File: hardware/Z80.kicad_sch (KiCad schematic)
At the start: 24 parts, among them J1 RP2040 SWD, SW1 Reset, U1 Pico, U2 SN74HC165N, U3 SN74HC165N, U4 Z80CPU

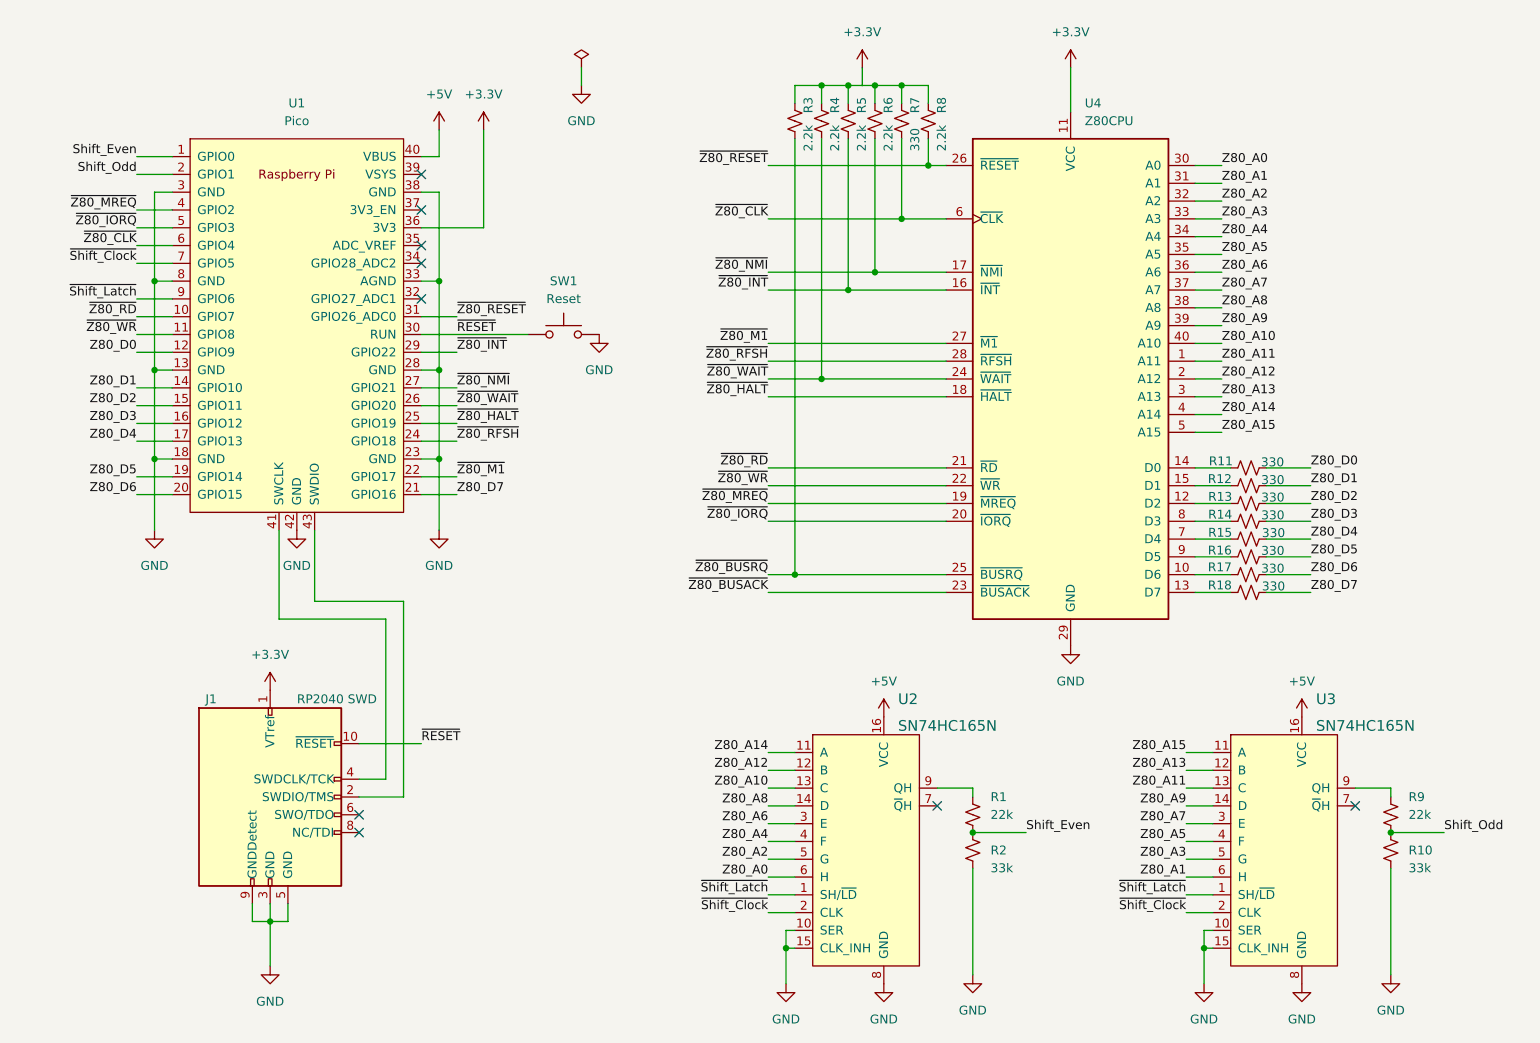
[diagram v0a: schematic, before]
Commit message: Initial firmware commit
This is a simple little program that makes sure that the RP2040 and its
PIO hardware can be used to clock the Z80 microprocessor and satisfy
its memory requests. It runs a simple Z80 program that increments a
16-bit counter in a loop and verifies that this counter is incremented
as expected.

* Updated README to cover the latest developments on this project.
* Updated schematic with changes that I found I had to make once I had
  it prototyped on a breadboard and started writing the PIO state
  machine code.
* Only running the Z80 at 1kHz with the firmware in this commit but it
  can run faster. The maximum frequency is currently limited by the
  shift registers and that is around 400kHz. The RP2040 code itself
  will probably introduce a limit somewhere between 2 and 3MHz.
* The code can be vastly improved but this code is far enough along
  that I feel it is safe for me to design a PCB around the current
  schematic and have it fabricated so that I move away from the
  breadboard implementation.
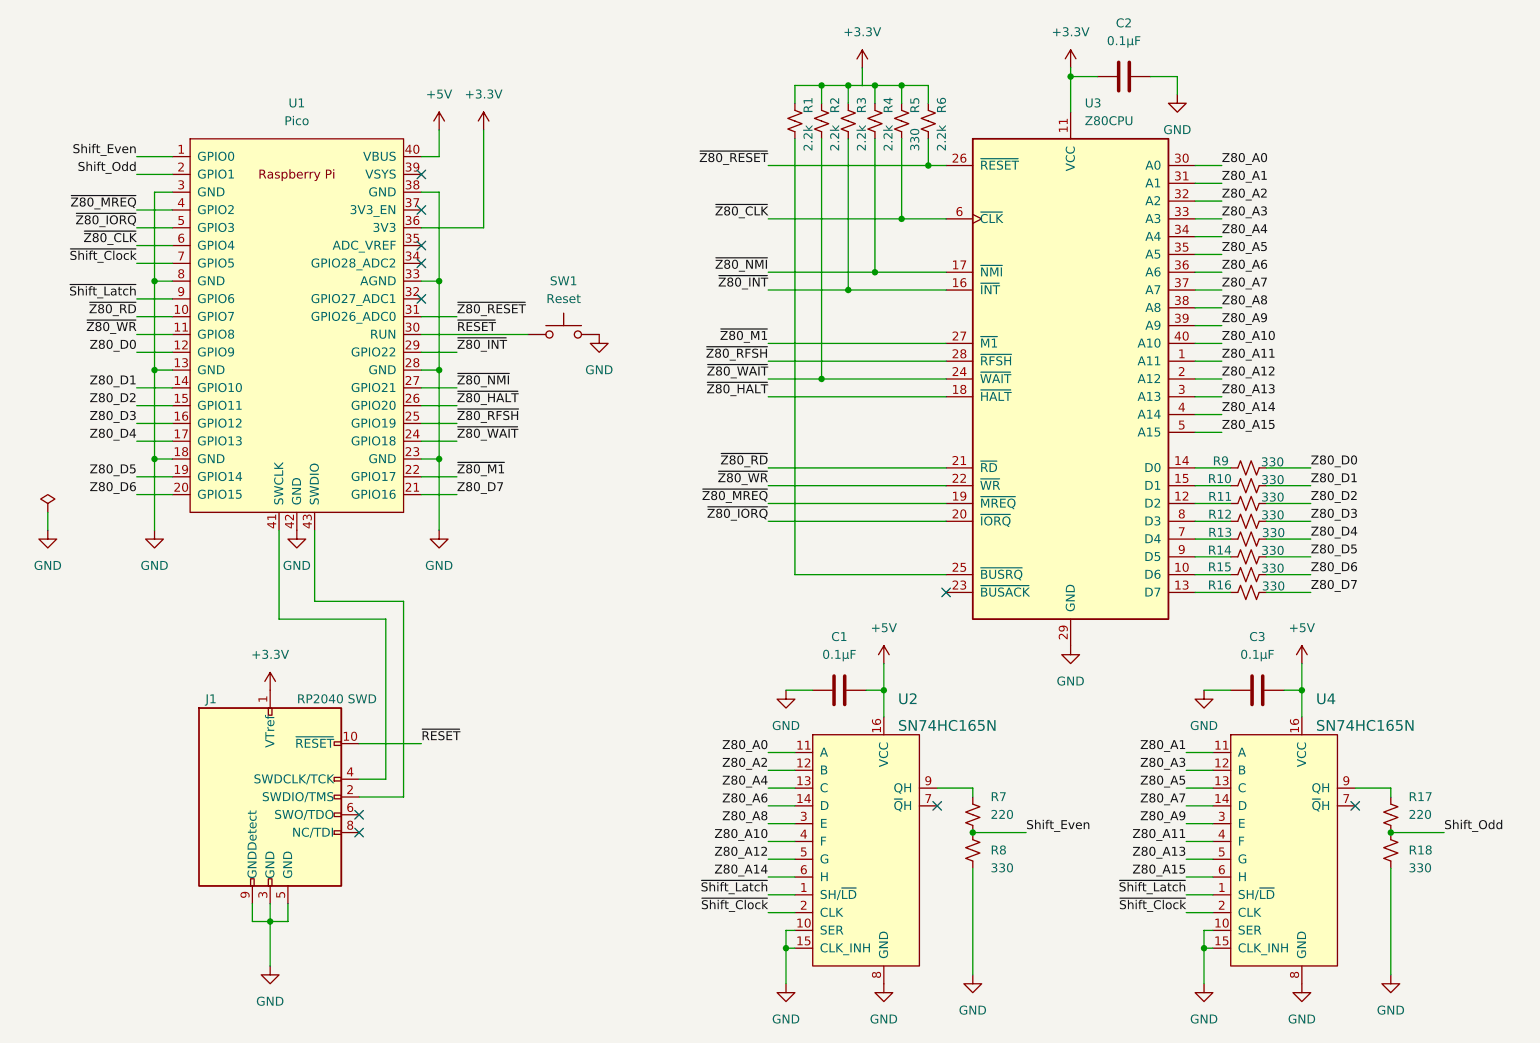
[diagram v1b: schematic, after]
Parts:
- added C1, C2, C3: 0.1µF, symbol Device:C
- R17: renamed from R9; value 22k -> 220
- R18: renamed from R10; value 33k -> 330
- R7: renamed from R1; value 22k -> 220
- R8: renamed from R2; value 33k -> 330
- renumbered R3 to R1, R12 to R10, R13 to R11, R14 to R12, R15 to R13, R16 to R14, R17 to R15, R18 to R16, R4 to R2, R5 to R3, R6 to R4, R7 to R5, R8 to R6, R11 to R9, U4 to U3, U3 to U4
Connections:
- net +3.3V: now also C2.1
- net +5V: now also C1.2, C3.2
- net GND: now also C1.1, C2.2, C3.1
- net Z80_A0: now also U2.11 (A); no longer U2.6 (H)
- net Z80_A1: now also U4.11 (A); no longer U4.6 (H)
- net Z80_A10: now also U2.4 (F); no longer U2.13 (C)
- net Z80_A11: now also U4.4 (F); no longer U4.13 (C)
- net Z80_A12: now also U2.5 (G); no longer U2.12 (B)
- net Z80_A13: now also U4.5 (G); no longer U4.12 (B)
- net Z80_A14: now also U2.6 (H); no longer U2.11 (A)
- net Z80_A15: now also U4.6 (H); no longer U4.11 (A)
- net Z80_A2: now also U2.12 (B); no longer U2.5 (G)
- net Z80_A3: now also U4.12 (B); no longer U4.5 (G)
- net Z80_A4: now also U2.13 (C); no longer U2.4 (F)
- net Z80_A5: now also U4.13 (C); no longer U4.4 (F)
- net Z80_A6: now also U2.14 (D); no longer U2.3 (E)
- net Z80_A7: now also U4.14 (D); no longer U4.3 (E)
- net Z80_A8: now also U2.3 (E); no longer U2.14 (D)
- net Z80_A9: now also U4.3 (E); no longer U4.14 (D)
- net ~{Z80_HALT}: now also U1.26 (GPIO20); no longer U1.25 (GPIO19)
- net ~{Z80_RFSH}: now also U1.25 (GPIO19); no longer U1.24 (GPIO18)
- net ~{Z80_WAIT}: now also U1.24 (GPIO18); no longer U1.26 (GPIO20)
- net ~{Z80_BUSACK}: no longer names the net of U3.23 (~{BUSACK})
- net ~{Z80_BUSRQ}: no longer names the net of R1.2, U3.25 (~{BUSRQ})
- no-connect marks 9 -> 10

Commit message: Update schematic
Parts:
- removed R5: 330, symbol Device:R_Small_US
- renumbered R11 to R10, R12 to R11, R13 to R12, R14 to R13, R15 to R14, R16 to R15, R17 to R16, R18 to R17, R6 to R5, R7 to R6, R8 to R7, R9 to R8, R10 to R9
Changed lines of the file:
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@@
   (junction (at 180.34 38.1) (diameter 0) (color 0 0 0 0)
   )
-  (junction (at 176.53 45.72) (diameter 0) (color 0 0 0 0)
-  )
   (junction (at 165.1 26.67) (diameter 0) (color 0 0 0 0)
   )
@@
   )
   (junction (at 168.91 26.67) (diameter 0) (color 0 0 0 0)
-  )
-  (junction (at 176.53 26.67) (diameter 0) (color 0 0 0 0)
   )
   (junction (at 160.02 149.86) (diameter 0) (color 0 0 0 0)
@@
     (stroke (width 0) (type default) (color 0 0 0 0))
   )
-  (wire (pts (xy 176.53 45.72) (xy 182.88 45.72))
-    (stroke (width 0) (type default) (color 0 0 0 0))
-  )
   (wire (pts (xy 110.49 36.83) (xy 110.49 33.02))
     (stroke (width 0) (type default) (color 0 0 0 0))
@@
     (stroke (width 0) (type default) (color 0 0 0 0))
   )
-  (wire (pts (xy 176.53 34.29) (xy 176.53 45.72))
-    (stroke (width 0) (type default) (color 0 0 0 0))
-  )
   (wire (pts (xy 217.17 134.62) (xy 220.98 134.62))
     (stroke (width 0) (type default) (color 0 0 0 0))
@@
     (stroke (width 0) (type default) (color 0 0 0 0))
   )
-  (wire (pts (xy 176.53 26.67) (xy 176.53 29.21))
-    (stroke (width 0) (type default) (color 0 0 0 0))
-  )
   (wire (pts (xy 157.48 124.46) (xy 161.29 124.46))
     (stroke (width 0) (type default) (color 0 0 0 0))
@@
     (stroke (width 0) (type default) (color 0 0 0 0))
   )
-  (wire (pts (xy 176.53 26.67) (xy 172.72 26.67))
+  (wire (pts (xy 172.72 26.67) (xy 180.34 26.67))
     (stroke (width 0) (type default) (color 0 0 0 0))
   )
@@
     (stroke (width 0) (type default) (color 0 0 0 0))
   )
-  (wire (pts (xy 180.34 26.67) (xy 176.53 26.67))
-    (stroke (width 0) (type default) (color 0 0 0 0))
-  )
   (wire (pts (xy 157.48 127) (xy 161.29 127))
     (stroke (width 0) (type default) (color 0 0 0 0))
@@
     (stroke (width 0) (type default) (color 0 0 0 0))
   )
-  (wire (pts (xy 157.48 45.72) (xy 176.53 45.72))
+  (wire (pts (xy 157.48 45.72) (xy 182.88 45.72))
     (stroke (width 0) (type default) (color 0 0 0 0))
   )
@@
   (symbol (lib_id "Device:R_Small_US") (at 226.06 83.82 90) (unit 1)
     (in_bom yes) (on_board yes)
-    (property "Reference" "R10" (id 0) (at 221.9687 82.8574 90))
+    (property "Reference" "R9" (id 0) (at 221.9687 82.8574 90))
     (property "Value" "330" (id 1) (at 229.5364 82.9985 90))
     (property "Footprint" "" (id 2) (at 226.06 83.82 0)
@@
   (symbol (lib_id "Device:R_Small_US") (at 226.06 99.06 90) (unit 1)
     (in_bom yes) (on_board yes)
-    (property "Reference" "R16" (id 0) (at 221.9687 98.0399 90))
+    (property "Reference" "R15" (id 0) (at 221.9687 98.0399 90))
     (property "Value" "330" (id 1) (at 229.6304 98.1809 90))
     (property "Footprint" "" (id 2) (at 226.06 99.06 0)
@@
   (symbol (lib_id "Device:R_Small_US") (at 246.38 135.89 0) (unit 1)
     (in_bom yes) (on_board yes)
-    (property "Reference" "R18" (id 0) (at 248.92 135.89 0)
+    (property "Reference" "R17" (id 0) (at 248.92 135.89 0)
       (effects (font (size 1.27 1.27)) (justify left))
     )
@@
   (symbol (lib_id "Device:R_Small_US") (at 186.69 135.89 0) (unit 1)
     (in_bom yes) (on_board yes)
-    (property "Reference" "R8" (id 0) (at 189.23 135.89 0)
+    (property "Reference" "R7" (id 0) (at 189.23 135.89 0)
       (effects (font (size 1.27 1.27)) (justify left))
     )
@@
   (symbol (lib_id "Device:R_Small_US") (at 180.34 31.75 0) (unit 1)
     (in_bom yes) (on_board yes)
-    (property "Reference" "R6" (id 0) (at 182.259 30.6376 90)
+    (property "Reference" "R5" (id 0) (at 182.259 30.6376 90)
       (effects (font (size 1.27 1.27)) (justify left))
     )
@@
   (symbol (lib_id "Device:R_Small_US") (at 226.06 81.28 90) (unit 1)
     (in_bom yes) (on_board yes)
-    (property "Reference" "R9" (id 0) (at 222.1097 80.3192 90))
+    (property "Reference" "R8" (id 0) (at 222.1097 80.3192 90))
     (property "Value" "330" (id 1) (at 229.4894 80.4602 90))
     (property "Footprint" "" (id 2) (at 226.06 81.28 0)
@@
   (symbol (lib_id "Device:R_Small_US") (at 226.06 86.36 90) (unit 1)
     (in_bom yes) (on_board yes)
-    (property "Reference" "R11" (id 0) (at 222.0157 85.3957 90))
+    (property "Reference" "R10" (id 0) (at 222.0157 85.3957 90))
     (property "Value" "330" (id 1) (at 229.5364 85.4897 90))
     (property "Footprint" "" (id 2) (at 226.06 86.36 0)
@@
   (symbol (lib_id "Device:R_Small_US") (at 226.06 96.52 90) (unit 1)
     (in_bom yes) (on_board yes)
-    (property "Reference" "R15" (id 0) (at 221.9687 95.4547 90))
+    (property "Reference" "R14" (id 0) (at 221.9687 95.4547 90))
     (property "Value" "330" (id 1) (at 229.5364 95.6427 90))
     (property "Footprint" "" (id 2) (at 226.06 96.52 0)
@@
   (symbol (lib_id "Device:R_Small_US") (at 186.69 130.81 0) (unit 1)
     (in_bom yes) (on_board yes)
-    (property "Reference" "R7" (id 0) (at 189.23 128.27 0)
+    (property "Reference" "R6" (id 0) (at 189.23 128.27 0)
       (effects (font (size 1.27 1.27)) (justify left))
     )
@@
   (symbol (lib_id "Device:R_Small_US") (at 226.06 93.98 90) (unit 1)
     (in_bom yes) (on_board yes)
-    (property "Reference" "R14" (id 0) (at 221.9687 93.0574 90))
+    (property "Reference" "R13" (id 0) (at 221.9687 93.0574 90))
     (property "Value" "330" (id 1) (at 229.5364 93.1044 90))
     (property "Footprint" "" (id 2) (at 226.06 93.98 0)
@@
     (pin "1")
   )
-  (symbol (lib_id "Device:R_Small_US") (at 176.53 31.75 0) (unit 1)
-    (in_bom yes) (on_board yes)
-    (property "Reference" "R5" (id 0) (at 178.449 30.6376 90)
-      (effects (font (size 1.27 1.27)) (justify left))
-    )
-    (property "Value" "330" (id 1) (at 178.449 36.0748 90)
-      (effects (font (size 1.27 1.27)) (justify left))
-    )
-    (property "Footprint" "" (id 2) (at 176.53 31.75 0)
-      (effects (font (size 1.27 1.27)) hide)
-    )
-    (property "Datasheet" "~" (id 3) (at 176.53 31.75 0)
-      (effects (font (size 1.27 1.27)) hide)
-    )
-    (pin "1")
-    (pin "2")
-  )
   (symbol (lib_id "Device:R_Small_US") (at 226.06 91.44 90) (unit 1)
     (in_bom yes) (on_board yes)
-    (property "Reference" "R13" (id 0) (at 222.0157 90.5192 90))
+    (property "Reference" "R12" (id 0) (at 222.0157 90.5192 90))
     (property "Value" "330" (id 1) (at 229.6304 90.5662 90))
     (property "Footprint" "" (id 2) (at 226.06 91.44 0)
@@
   (symbol (lib_id "Device:R_Small_US") (at 246.38 130.81 0) (unit 1)
     (in_bom yes) (on_board yes)
-    (property "Reference" "R17" (id 0) (at 248.92 128.27 0)
+    (property "Reference" "R16" (id 0) (at 248.92 128.27 0)
       (effects (font (size 1.27 1.27)) (justify left))
     )
@@
   (symbol (lib_id "Device:R_Small_US") (at 226.06 88.9 90) (unit 1)
     (in_bom yes) (on_board yes)
-    (property "Reference" "R12" (id 0) (at 222.0157 87.9339 90))
+    (property "Reference" "R11" (id 0) (at 222.0157 87.9339 90))
     (property "Value" "330" (id 1) (at 229.5364 88.0279 90))
     (property "Footprint" "" (id 2) (at 226.06 88.9 0)
@@
       (reference "R4") (unit 1) (value "2.2k") (footprint "")
     )
-    (path "/cb47eb21-f040-4a40-a689-d6b0ddf769fa"
-      (reference "R5") (unit 1) (value "330") (footprint "")
-    )
     (path "/4d5dd215-58fa-42fb-b48d-aae8a2cb4b7b"
-      (reference "R6") (unit 1) (value "2.2k") (footprint "")
+      (reference "R5") (unit 1) (value "2.2k") (footprint "")
     )
     (path "/ab03a96a-589d-4905-bd0c-4425f3417fb6"
-      (reference "R7") (unit 1) (value "220") (footprint "")
+      (reference "R6") (unit 1) (value "220") (footprint "")
     )
     (path "/4c05fbcf-e16b-4fd5-a5b1-a43636fa6dc3"
+      (reference "R7") (unit 1) (value "330") (footprint "")
+    )
+    (path "/5bae8d7f-a215-4306-b303-12041ae1d9dd"
       (reference "R8") (unit 1) (value "330") (footprint "")
     )
-    (path "/5bae8d7f-a215-4306-b303-12041ae1d9dd"
+    (path "/29967022-0716-413a-ae37-d82856be92e4"
       (reference "R9") (unit 1) (value "330") (footprint "")
     )
-    (path "/29967022-0716-413a-ae37-d82856be92e4"
+    (path "/96e68a8f-6e74-4e08-8f85-1adc6029fb52"
       (reference "R10") (unit 1) (value "330") (footprint "")
     )
-    (path "/96e68a8f-6e74-4e08-8f85-1adc6029fb52"
+    (path "/ff2ab6fa-a536-41a2-967e-8798d3665a42"
       (reference "R11") (unit 1) (value "330") (footprint "")
     )
-    (path "/ff2ab6fa-a536-41a2-967e-8798d3665a42"
+    (path "/cfa47cbe-c711-4d7b-b1fb-ed6f496e968d"
       (reference "R12") (unit 1) (value "330") (footprint "")
     )
-    (path "/cfa47cbe-c711-4d7b-b1fb-ed6f496e968d"
+    (path "/b3a77dbd-5397-4860-86c3-f296c00c8887"
       (reference "R13") (unit 1) (value "330") (footprint "")
     )
-    (path "/b3a77dbd-5397-4860-86c3-f296c00c8887"
+    (path "/a67dbef9-d4bd-4d26-9e93-58134f77470d"
       (reference "R14") (unit 1) (value "330") (footprint "")
     )
-    (path "/a67dbef9-d4bd-4d26-9e93-58134f77470d"
+    (path "/2aedb671-8989-4b47-ad64-1185ff3636e4"
       (reference "R15") (unit 1) (value "330") (footprint "")
     )
-    (path "/2aedb671-8989-4b47-ad64-1185ff3636e4"
-      (reference "R16") (unit 1) (value "330") (footprint "")
-    )
     (path "/dd4d79f8-b127-407e-b0f5-84fb8ae6cf5e"
-      (reference "R17") (unit 1) (value "220") (footprint "")
+      (reference "R16") (unit 1) (value "220") (footprint "")
     )
     (path "/46a5f6c5-58e2-4a38-b05a-906ac03e993f"
-      (reference "R18") (unit 1) (value "330") (footprint "")
+      (reference "R17") (unit 1) (value "330") (footprint "")
     )
     (path "/43f2995b-d916-4d25-9b53-e4118a2ec730"

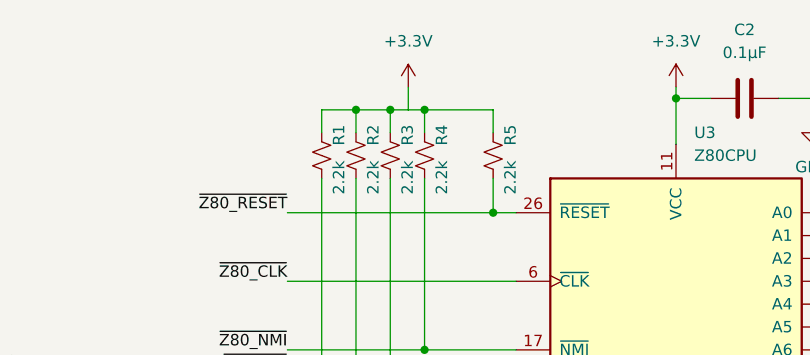
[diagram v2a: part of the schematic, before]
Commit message: Initial PCB design
* Designed version 1.1 of the PCB and sent it off to OSHPark to have it
  fabricated.
* Fixed a missing connection between 3.3V and a bunch of Z80 pull-ups
  that I had in my schematic that I didn't notice until I was working
  on the PCB.
* Updated README with the latest project progression.
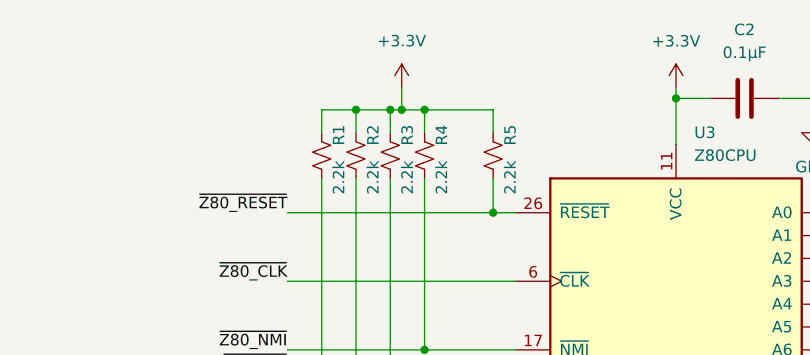
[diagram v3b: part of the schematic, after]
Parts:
- C1, C2, C3: footprint (none) -> Capacitor_SMD:C_0805_2012Metric_Pad1.18x1.45mm_HandSolder
- J1: footprint (none) -> SWD_footprints:CON10_2X5_DUK_FTSH_SAI
- R1, R10, R11, R12, R13, R14, R15, R16, R17, R2, R3, R4, R5, R6, R7, R8, R9: footprint (none) -> Resistor_SMD:R_0805_2012Metric_Pad1.20x1.40mm_HandSolder
- SW1: footprint (none) -> Button_Switch_SMD:SW_Push_1P1T_NO_6x6mm_H9.5mm
- U3: footprint (none) -> Package_DIP:DIP-40_W15.24mm
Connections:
- net +3.3V: now also R1.1, R2.1, R3.1, R4.1, R5.1
